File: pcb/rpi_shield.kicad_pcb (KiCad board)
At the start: 2 copper layers, 65 x 56 mm, 41 parts, among them P101 CONN_01X08, P102 CONN_02X20, P301 USB_OTG, Q201 Q_NMOS_GDSD, Q202 Q_NMOS_GDSD, Q203 Q_NMOS_GDSD, Q204 Q_NMOS_GDSD, Q301 FT230XS-R, U201 LM2902N, U202 MAX5813

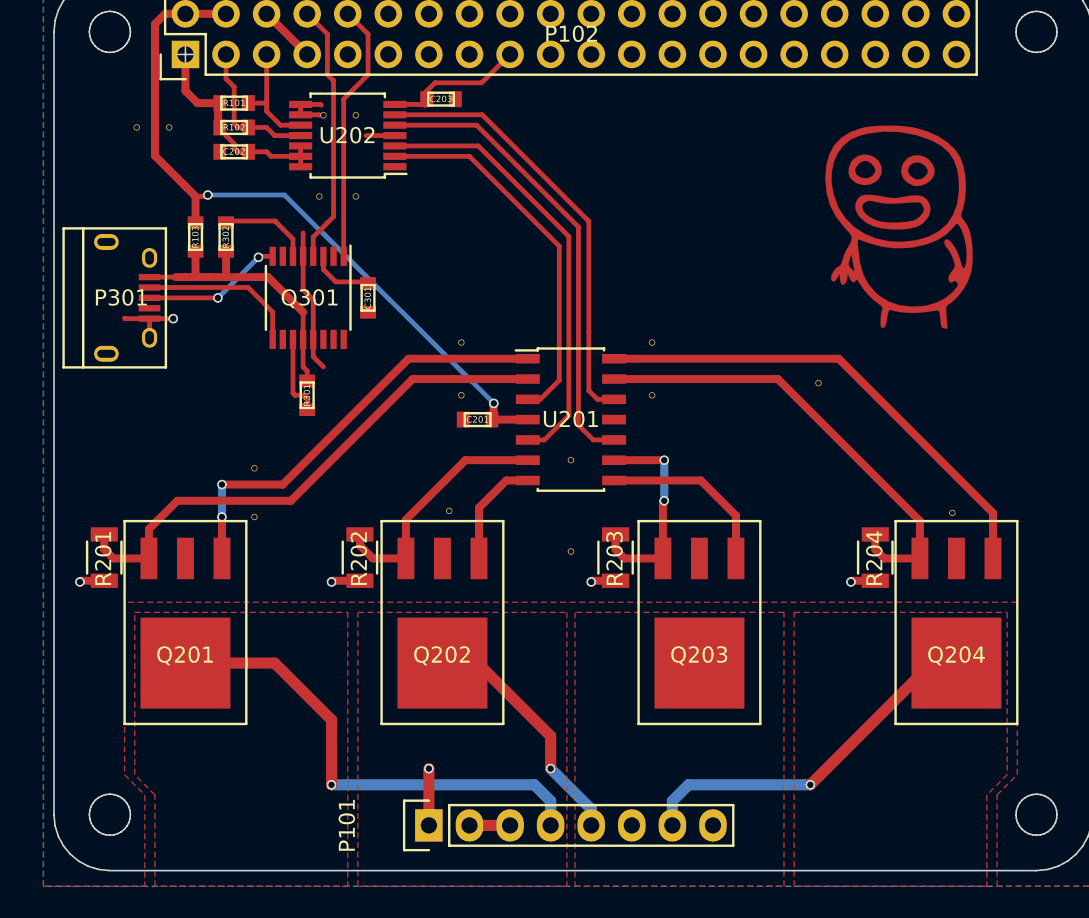
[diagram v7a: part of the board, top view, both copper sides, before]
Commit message: moved usb header, rerouted a few traces
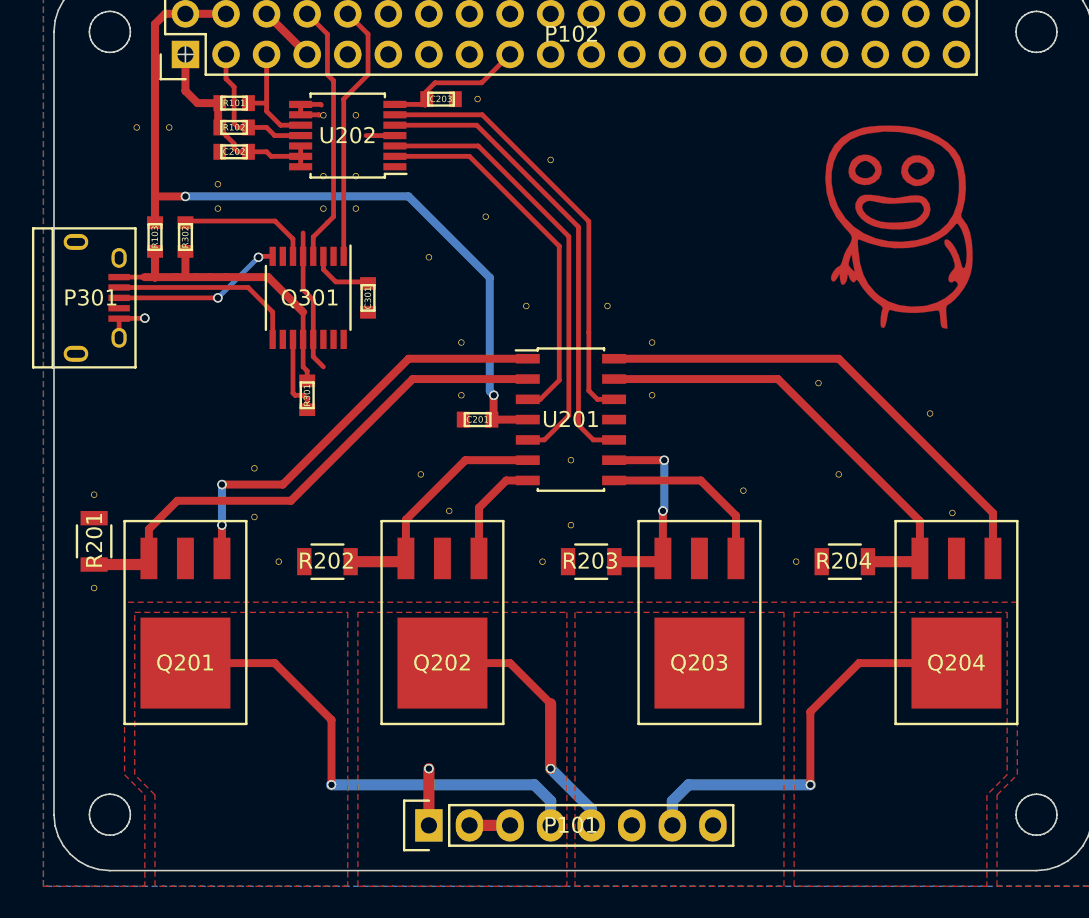
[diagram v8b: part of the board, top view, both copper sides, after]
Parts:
- added VIA: via, netl:via, F.Cu at (145.2, 92.7)
- added VIA: via, netl:via, F.Cu at (124.3, 107.6)
- added VIA: via, netl:via, F.Cu at (144.7, 106.3)
- added VIA: via, netl:via, F.Cu at (148.8, 90.2)
- added VIA: via, netl:via, F.Cu at (152.9, 86.6)
- added VIA: via, netl:via, F.Cu at (156.4, 95.7)
- added VIA: via, netl:via, F.Cu at (151.3, 95.7)
- added VIA: via, netl:via, F.Cu at (148.3, 82.8)
- added VIA: via, netl:via, F.Cu at (164.9, 107.3)
- added VIA: via, netl:via, F.Cu at (170.9, 106.3)
- added VIA: via, netl:via, F.Cu at (176.6, 102.5)
- added VIA: via, netl:via, F.Cu at (132.0, 88.1)
- added VIA: via, netl:via, F.Cu at (132.0, 89.7)
- added VIA: via, netl:via, F.Cu at (140.7, 87.6)
- added VIA: via, netl:via, F.Cu at (138.6, 87.6)
- added VIA: via, netl:via, F.Cu at (135.8, 111.8)
- added VIA: via, netl:via, F.Cu at (168.2, 111.8)
- added VIA: via, netl:via, F.Cu at (152.4, 111.8)
- added VIA: via, netl:via, F.Cu at (124.3, 113.4)
- moved R103 2.54 mm to (128.1, 91.4)
- moved R302 2.54 mm to (130.0, 91.4)
- moved R202 2.05 mm to (138.9, 111.8), turned to 180 degrees
- moved R204 1.92 mm to (171.3, 111.8), turned to 180 degrees
- moved P301 1.91 mm to (124.3, 95.2)
- moved VIA 1.65 mm to (154.1, 109.5)
- moved R203 1.55 mm to (155.4, 111.8), turned to 180 degrees
- moved R201 1.20 mm to (124.3, 110.5), turned to 90 degrees
- moved VIA 0.80 mm to (138.6, 89.7)
- moved VIA 0.76 mm to (140.7, 89.7)
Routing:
- net GND: track 31.9 -> 24.3 mm, vias 6 -> 2
- net 5V: track 45.4 -> 51.2 mm
- net /LED driver/DrainFan: track 22.9 -> 27.1 mm
- net Net-(Q301-Pad6): track 5.74 -> 8.28 mm
- net /USBSerial/5VUSB: track 17.9 -> 19.8 mm
- net Net-(P301-Pad3): track 8.79 -> 10.7 mm
- net Net-(P301-Pad2): track 10.1 -> 12.0 mm
- net /LED driver/DrainGreen: track 15.3 -> 16.5 mm
- net Net-(Q203-Pad3): track 14.6 -> 13.5 mm
- net Net-(Q204-Pad3): track 29.8 -> 29.2 mm
